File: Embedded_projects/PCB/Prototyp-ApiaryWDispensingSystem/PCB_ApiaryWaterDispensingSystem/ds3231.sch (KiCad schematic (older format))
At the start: 1 part

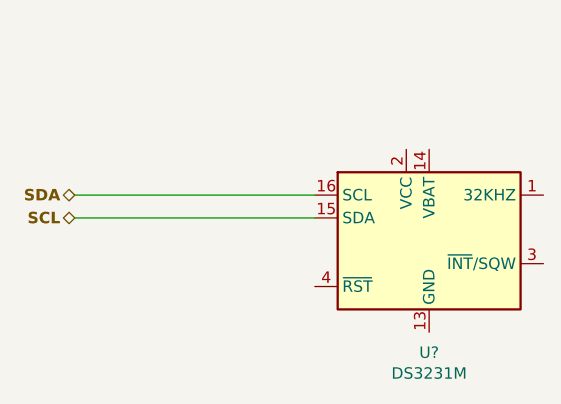
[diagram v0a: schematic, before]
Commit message: added BME280 sensor to the project , #3
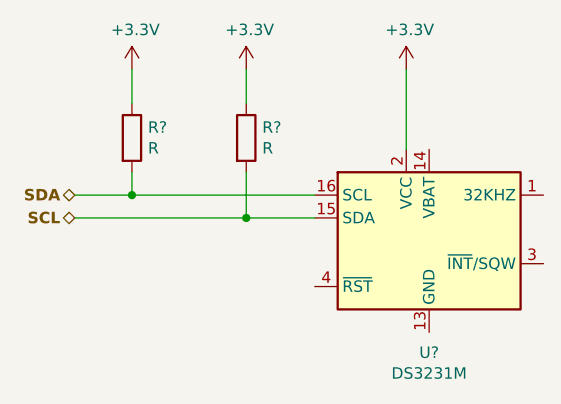
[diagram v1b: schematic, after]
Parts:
- added R? (x2): R, symbol Device:R
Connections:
- net SCL: now also R?.2
- net SDA: now also R?.2
- net +3V3: now reaches U?.2 (VCC)
- net +3V3: now also R?.1, R?.1
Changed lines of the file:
@@
 SCL
 Wire Wire Line
-	2600 2100 3650 2100
+	2600 2100 2850 2100
 Wire Wire Line
-	2600 2200 3650 2200
+	2600 2200 3350 2200
+$Comp
+L power:+3.3V #PWR?
+U 1 1 67D4B950
+P 2850 1550
+F 0 "#PWR?" H 2850 1400 50  0001 C CNN
+F 1 "+3.3V" H 2865 1723 50  0000 C CNN
+F 2 "" H 2850 1550 50  0001 C CNN
+F 3 "" H 2850 1550 50  0001 C CNN
+	1    2850 1550
+	1    0    0    -1
+$EndComp
+$Comp
+L Device:R R?
+U 1 1 67D4C7E4
+P 2850 1850
+F 0 "R?" H 2920 1896 50  0000 L CNN
+F 1 "R" H 2920 1805 50  0000 L CNN
+F 2 "" V 2780 1850 50  0001 C CNN
+F 3 "~" H 2850 1850 50  0001 C CNN
+	1    2850 1850
+	1    0    0    -1
+$EndComp
+$Comp
+L Device:R R?
+U 1 1 67D4CD68
+P 3350 1850
+F 0 "R?" H 3420 1896 50  0000 L CNN
+F 1 "R" H 3420 1805 50  0000 L CNN
+F 2 "" V 3280 1850 50  0001 C CNN
+F 3 "~" H 3350 1850 50  0001 C CNN
+	1    3350 1850
+	1    0    0    -1
+$EndComp
+$Comp
+L power:+3.3V #PWR?
+U 1 1 67D4D759
+P 3350 1550
+F 0 "#PWR?" H 3350 1400 50  0001 C CNN
+F 1 "+3.3V" H 3365 1723 50  0000 C CNN
+F 2 "" H 3350 1550 50  0001 C CNN
+F 3 "" H 3350 1550 50  0001 C CNN
+	1    3350 1550
+	1    0    0    -1
+$EndComp
+Wire Wire Line
+	3350 1550 3350 1700
+Wire Wire Line
+	2850 1550 2850 1700
+Wire Wire Line
+	3350 2000 3350 2200
+Connection ~ 3350 2200
+Wire Wire Line
+	3350 2200 3650 2200
+Wire Wire Line
+	2850 2000 2850 2100
+Connection ~ 2850 2100
+Wire Wire Line
+	2850 2100 3650 2100
+$Comp
+L power:+3.3V #PWR?
+U 1 1 67D4E539
+P 4050 1550
+F 0 "#PWR?" H 4050 1400 50  0001 C CNN
+F 1 "+3.3V" H 4065 1723 50  0000 C CNN
+F 2 "" H 4050 1550 50  0001 C CNN
+F 3 "" H 4050 1550 50  0001 C CNN
+	1    4050 1550
+	1    0    0    -1
+$EndComp
+Wire Wire Line
+	4050 1900 4050 1550
 $EndSCHEMATC
